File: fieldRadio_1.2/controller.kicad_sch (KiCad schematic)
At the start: 64 parts, among them J11 Conn_01x04, Q19 BSS138, U31 MIC5235-3.3YM5, Y1 32.768kHz

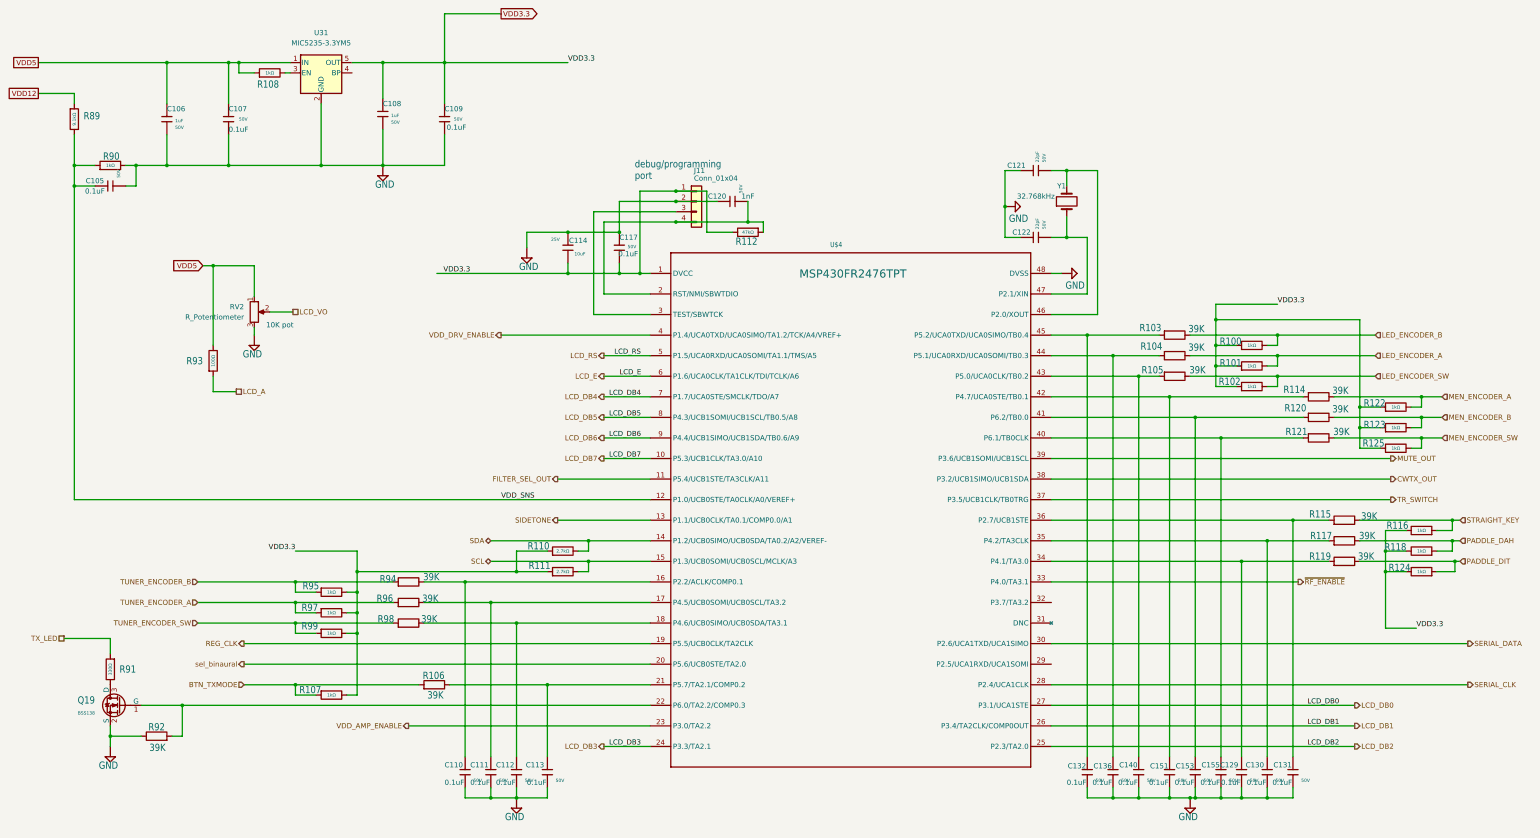
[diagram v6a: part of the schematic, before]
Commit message: Starting fieldRadio1.2 layout
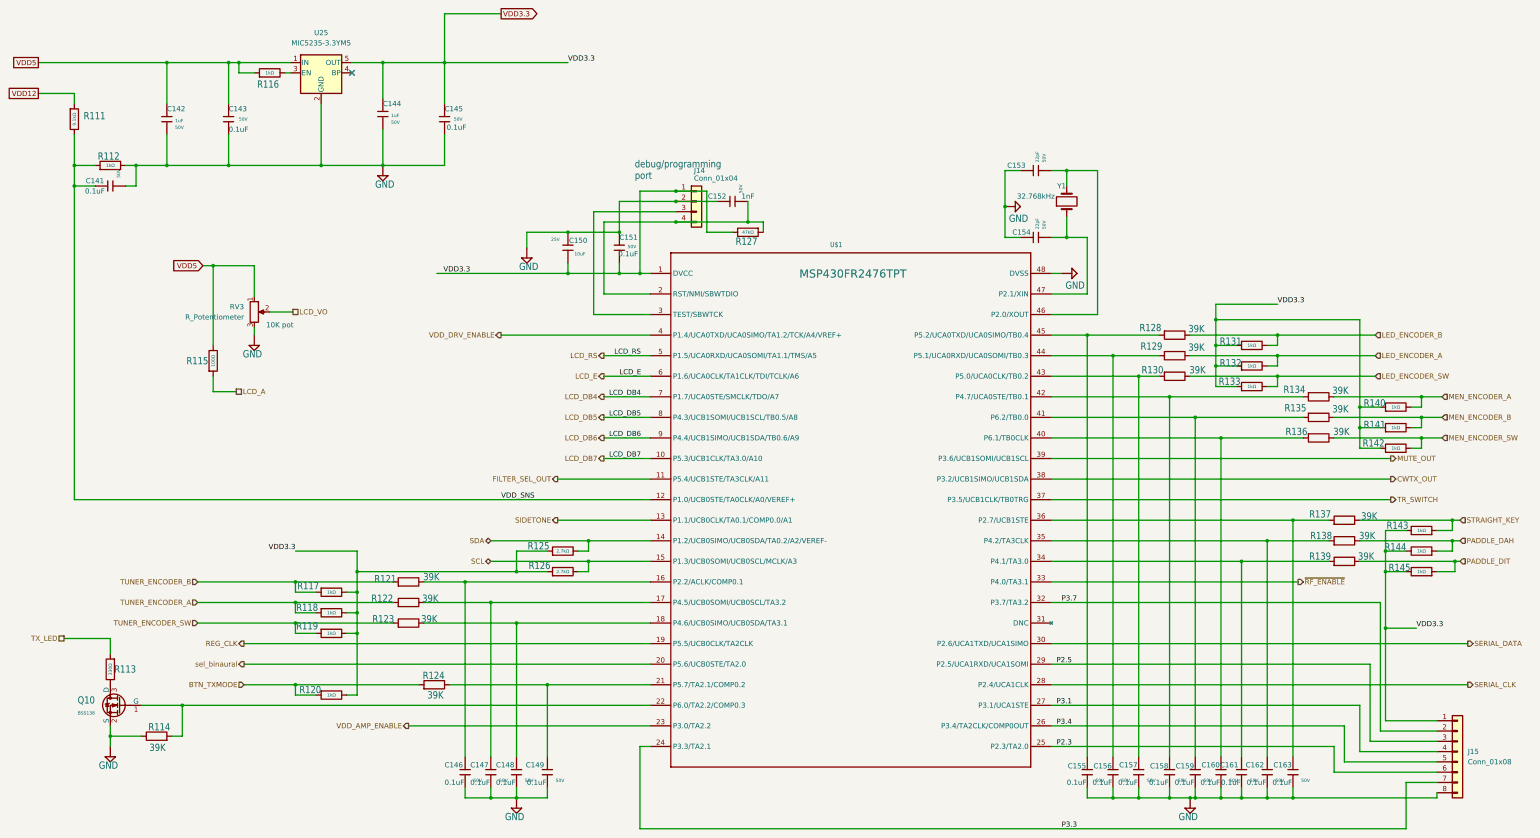
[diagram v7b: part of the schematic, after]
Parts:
- removed RV2: R_Potentiometer, Potentiometer_THT:Potentiometer_Bourns_3386C_Horizontal, symbol Device:R_Potentiometer
- added J15: Conn_01x08, Connector_PinHeader_2.54mm:PinHeader_1x08_P2.54mm_Vertical, symbol Connector_Generic:Conn_01x08
- added RV3: R_Potentiometer, Potentiometer_THT:Potentiometer_Bourns_3386C_Horizontal, symbol Device:R_Potentiometer
- renumbered C105 to C141, C106 to C142, C107 to C143, C108 to C144, C109 to C145, C110 to C146, C111 to C147, C112 to C148, C113 to C149, C114 to C150, C117 to C151, C120 to C152, C121 to C153, C122 to C154, C132 to C155, C136 to C156, C140 to C157, C151 to C158, C153 to C159, C155 to C160, C129 to C161, C130 to C162, C131 to C163, J11 to J14, Q19 to Q10, R89 to R111, R90 to R112, R91 to R113, R92 to R114, R93 to R115, R108 to R116, R95 to R117, R97 to R118, R99 to R119, R107 to R120, R94 to R121, R96 to R122, R98 to R123, R106 to R124, R110 to R125, R111 to R126, R112 to R127, R103 to R128, R104 to R129, R105 to R130, R100 to R131, R101 to R132, R102 to R133, R114 to R134, R120 to R135, R121 to R136, R115 to R137, R117 to R138, R119 to R139, R122 to R140, R123 to R141, R125 to R142, R116 to R143, R118 to R144, R124 to R145, U$4 to U$1, U31 to U25
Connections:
- net GND: now also J15.8 (Pin_8), RV3.3
- net LCD_VO: now also RV3.2
- net VDD3.3: now also J15.1 (Pin_1)
- net VDD5: now also RV3.1
- net P2.5: now reaches U$1.29 (P2.5/UCA1RXD/UCA1SOMI)
- net P2.5: now also J15.3 (Pin_3)
- net P3.7: now reaches U$1.32 (P3.7/TA3.2)
- net P3.7: now also J15.2 (Pin_2)
- net LCD_DB0 renamed P3.1
- net P3.1: now also J15.4 (Pin_4)
- net LCD_DB1 renamed P3.4
- net P3.4: now also J15.5 (Pin_5)
- net LCD_DB2 renamed P2.3
- net P2.3: now also J15.6 (Pin_6)
- net LCD_DB3 renamed P3.3
- net P3.3: now also J15.7 (Pin_7)
- no-connect marks 0 -> 1
